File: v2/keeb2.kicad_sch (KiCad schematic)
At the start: 34 parts, among them J1 AVR-ISP-6, J3 AudioJack4, SW2 SW_Push_Reset, SW71 RotaryEncoder_Switch, U1 ATmega32U4-A, Y1 XTAL

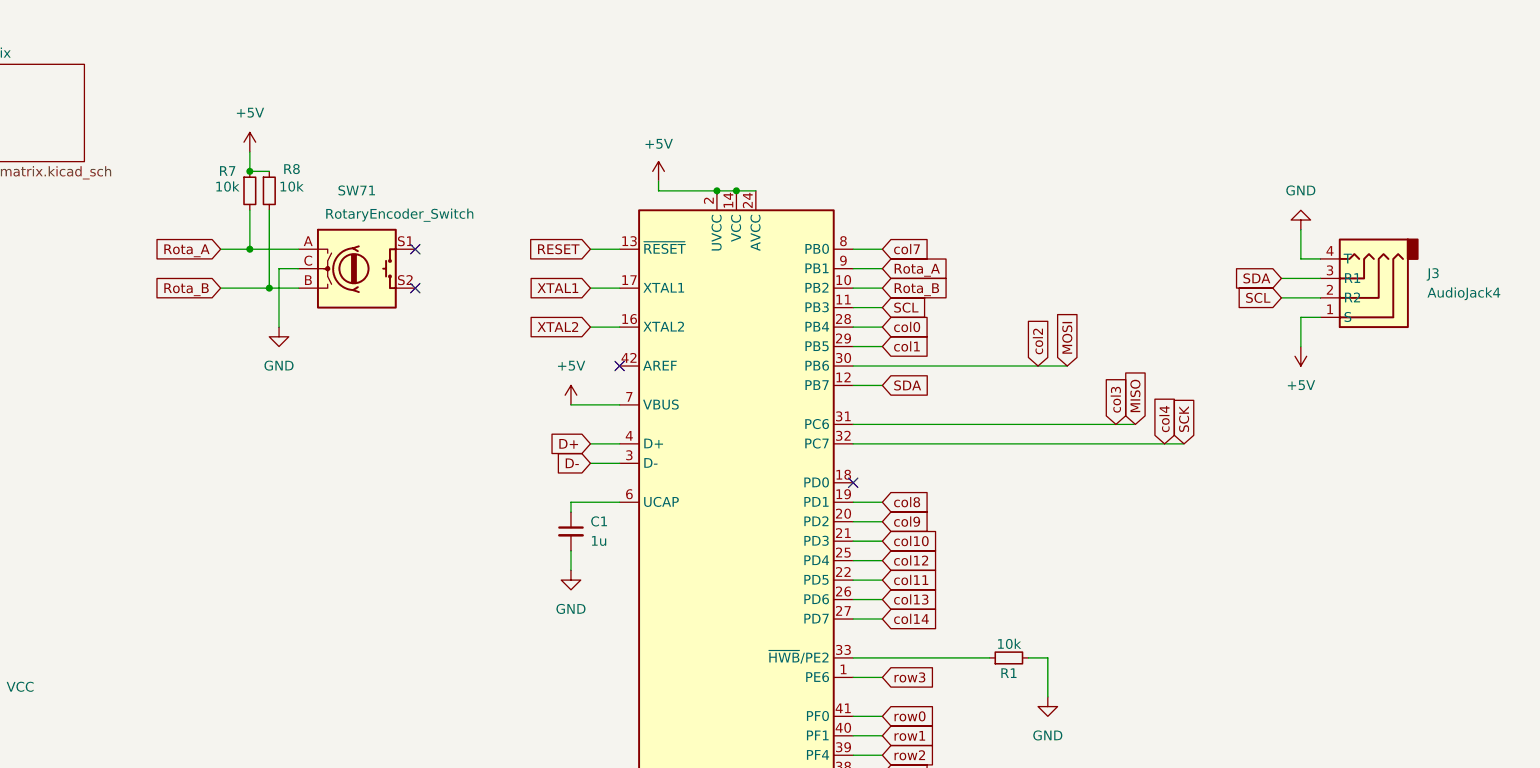
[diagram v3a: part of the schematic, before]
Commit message: squeeze keyboard in case
removed colomn 14 (4 keys), TTRS connection, and rotary encoder
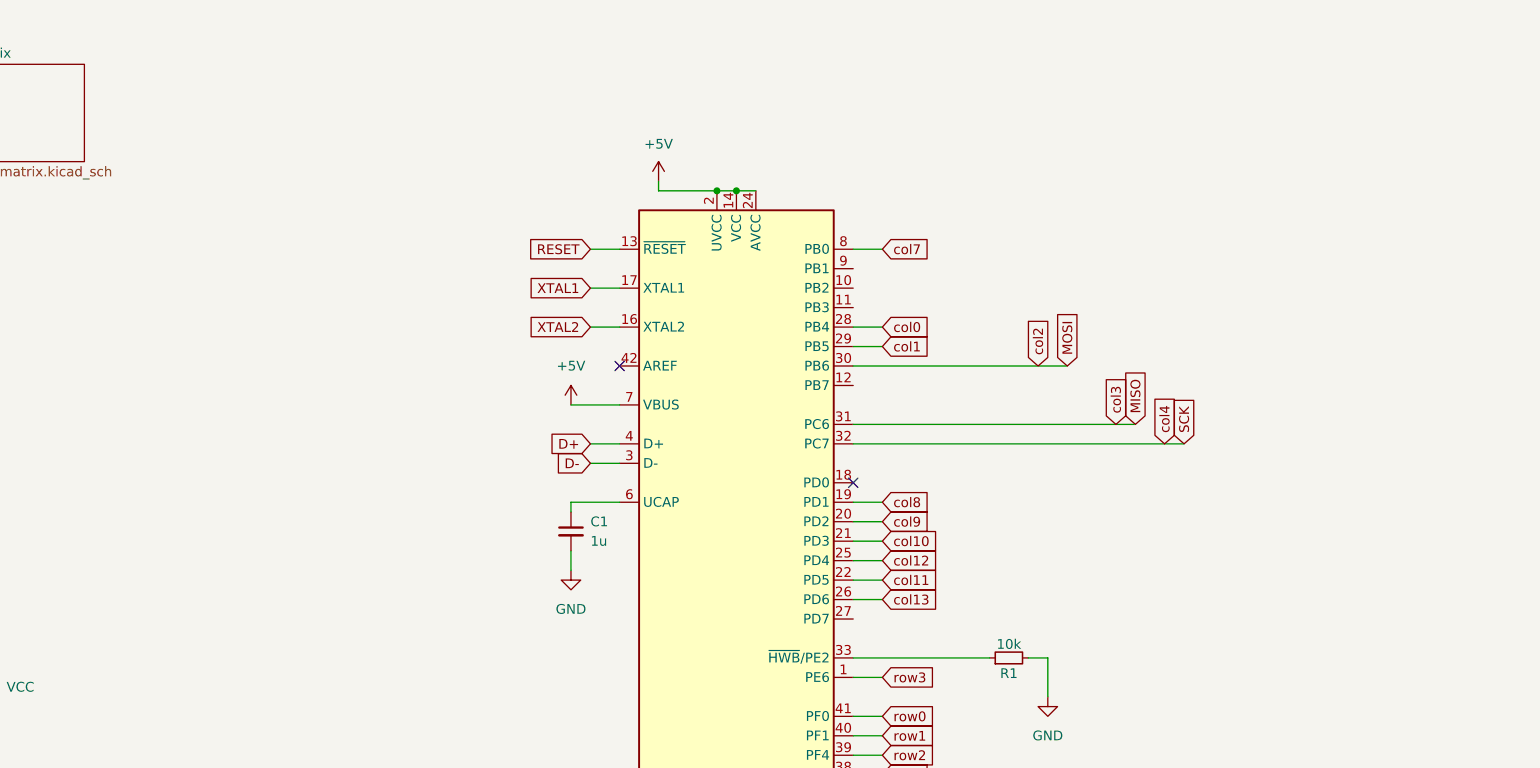
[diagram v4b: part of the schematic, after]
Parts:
- removed J3: AudioJack4, Keebio-Parts:TRRS-PJ-320A, symbol Connector_Audio:AudioJack4
- removed R7, R8: 10k, Resistor_SMD:R_0805_2012Metric_Pad1.20x1.40mm_HandSolder, symbol Device:R_Small
- removed SW71: RotaryEncoder_Switch, Keebio-Parts:RotaryEncoder_EC11, symbol Device:RotaryEncoder_Switch
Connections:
- net Rota_A: no longer names the net of U1.9 (PB1)
- net Rota_B: no longer names the net of U1.10 (PB2)
- net SCL: no longer names the net of U1.11 (PB3)
- net SDA: no longer names the net of U1.12 (PB7)
- net col14: no longer names the net of U1.27 (PD7)
- no-connect marks 6 -> 4

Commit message: Finished routing
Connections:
- net col8: now also U1.12 (PB7); no longer U1.19 (PD1)
- no-connect marks 4 -> 9
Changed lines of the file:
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@@
+	)
+	(no_connect
+		(at 210.82 49.53)
 	)
 	(no_connect
@@
 	)
 	(no_connect
+		(at 210.82 80.01)
+	)
+	(no_connect
+		(at 210.82 95.25)
+	)
+	(no_connect
+		(at 210.82 52.07)
+	)
+	(no_connect
 		(at 39.37 71.12)
 	)
+	(no_connect
+		(at 210.82 54.61)
+	)
 	(wire
 		(pts
@@
 	(wire
 		(pts
+			(xy 210.82 64.77) (xy 214.63 64.77)
+		)
+		(stroke
+			(width 0)
+			(type default)
+		)
+	)
+	(wire
+		(pts
 			(xy 193.04 134.62) (xy 195.58 134.62)
 		)
@@
 	(wire
 		(pts
-			(xy 210.82 80.01) (xy 214.63 80.01)
-		)
-		(stroke
-			(width 0)
-			(type default)
-		)
-	)
-	(wire
-		(pts
 			(xy 45.72 78.74) (xy 45.72 83.82)
 		)
@@
 		)
 	)
+	(global_label "col8"
+		(shape input)
+		(at 214.63 64.77 0)
+		(fields_autoplaced yes)
+		(effects
+			(font
+				(size 1.27 1.27)
+			)
+			(justify left)
+		)
+		(property "Intersheetrefs" "${INTERSHEET_REFS}"
+			(at 221.7275 64.77 0)
+			(effects
+				(font
+					(size 1.27 1.27)
+				)
+				(justify left)
+				(hide yes)
+			)
+		)
+	)
 	(global_label "col13"
 		(shape input)
@@
 				(hide yes)
 			)
-		)
-	)
-	(global_label "col8"
-		(shape input)
-		(at 214.63 80.01 0)
-		(fields_autoplaced yes)
-		(effects
-			(font
-				(size 1.27 1.27)
-			)
-			(justify left)
-		)
-		(property "Intersheetrefs" "${INTERSHEET_REFS}"
-			(at 221.7275 80.01 0)
-			(effects
-				(font
-					(size 1.27 1.27)
-				)
-				(justify left)
-				(hide yes)
-			)

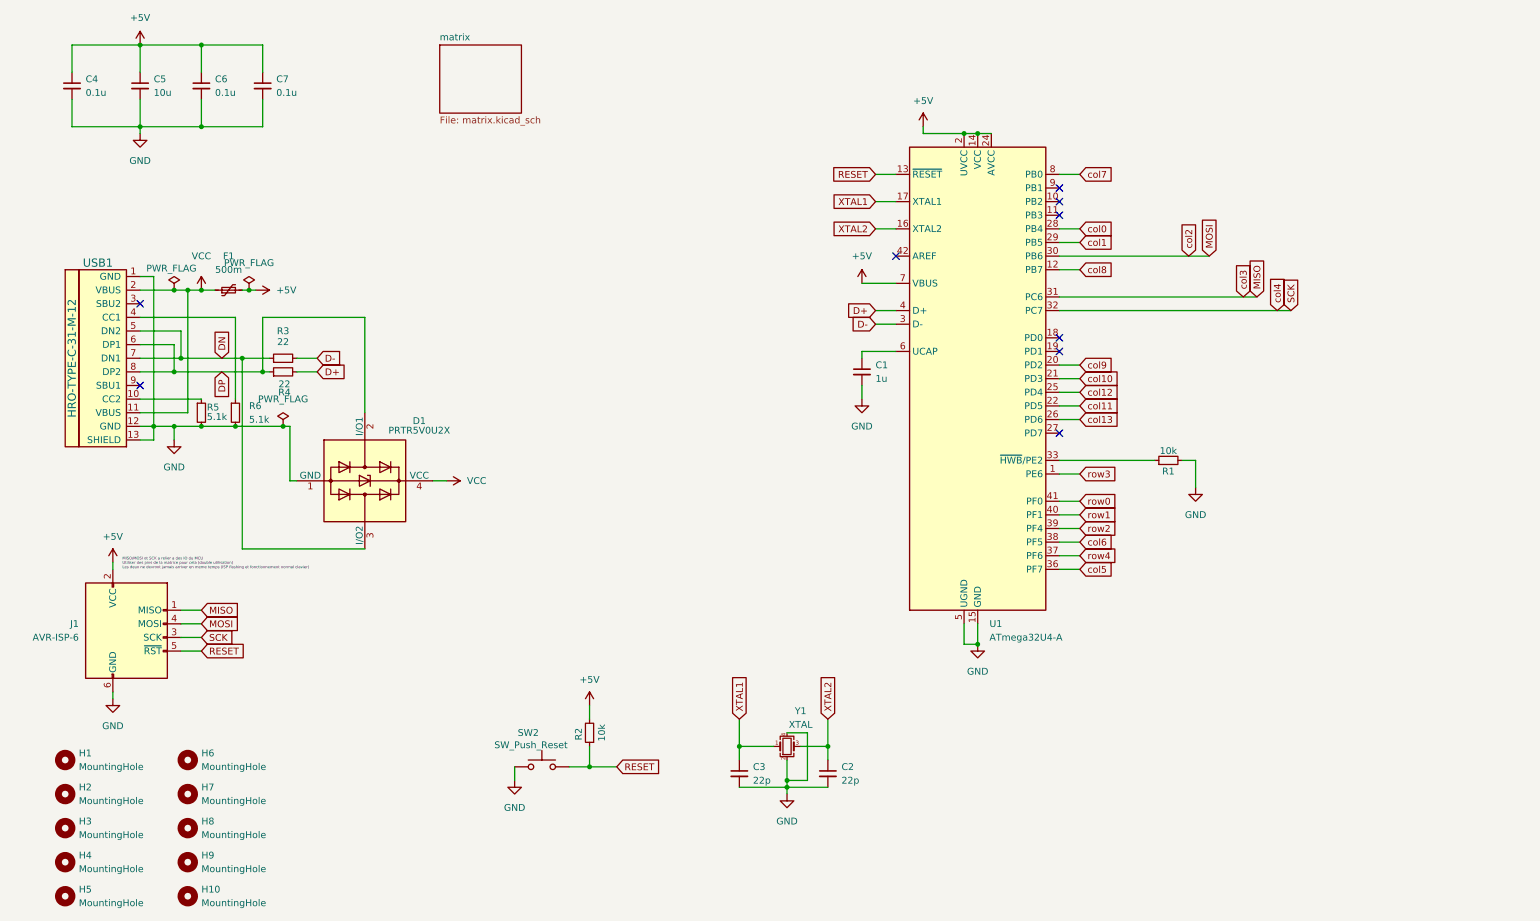
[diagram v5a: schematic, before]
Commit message: Added gnd layers and ferrite bead on USB
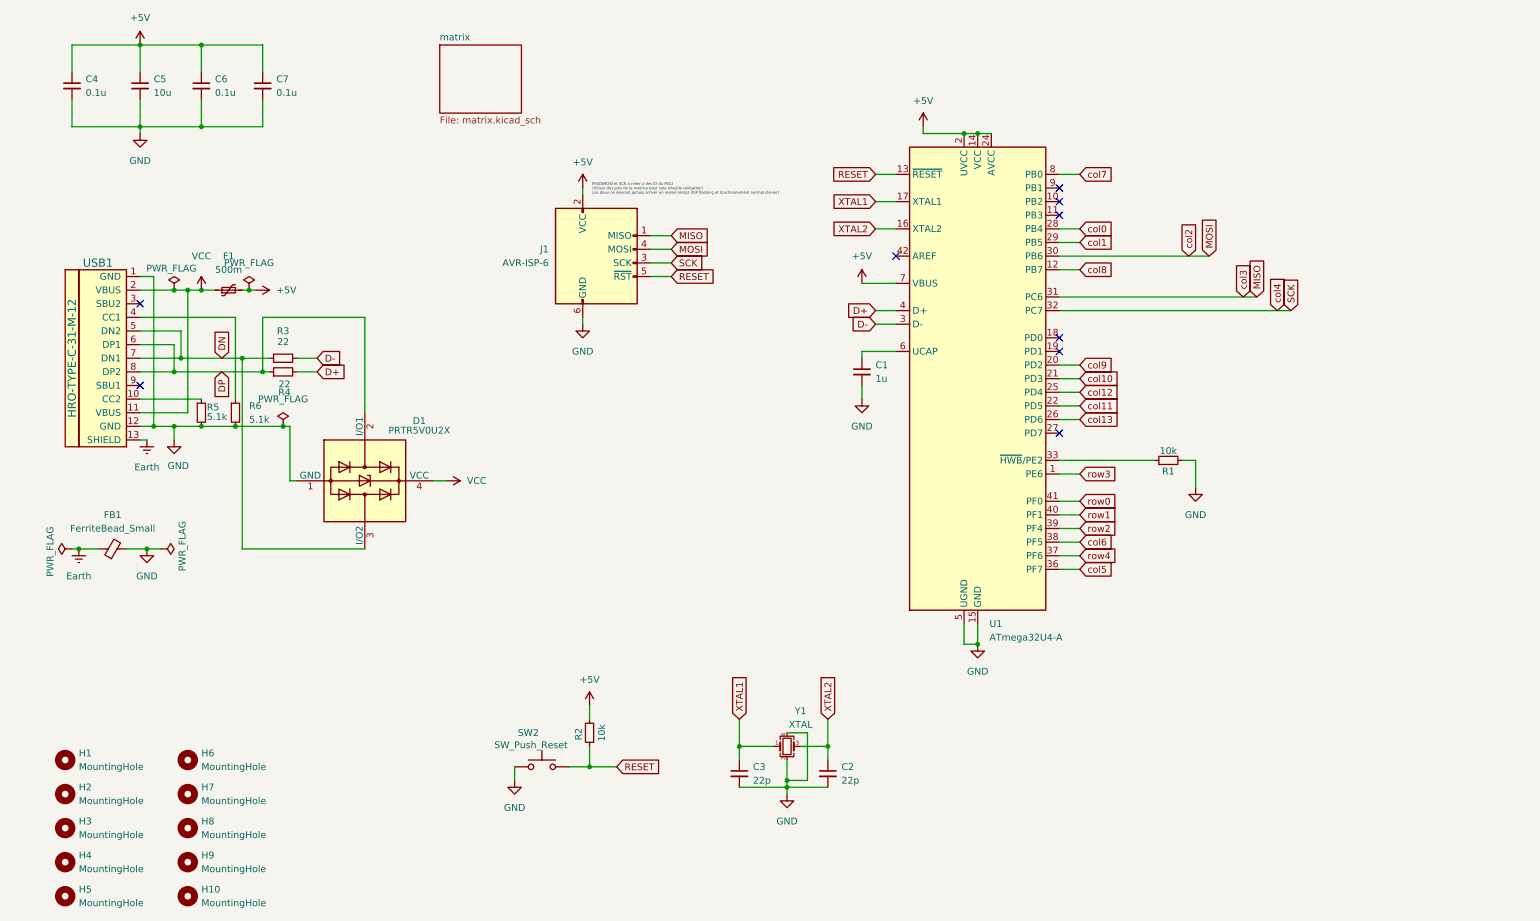
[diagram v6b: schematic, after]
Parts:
- added FB1: FerriteBead_Small, Inductor_SMD:L_0805_2012Metric_Pad1.15x1.40mm_HandSolder, symbol Device:FerriteBead_Small
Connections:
- net GND: now also FB1.2; no longer USB1.13 (SHIELD)
- new net Earth: FB1.1, USB1.13 (SHIELD)
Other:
- moved on the sheet: J1
